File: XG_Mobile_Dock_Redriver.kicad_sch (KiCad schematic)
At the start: 170 parts, among them J1 5-1775443-8, J13 39301240, J14 I2C1, J2 20455-040E-76, J3 20455-040E-76, J4 469911008, J7 10147430-113T0LF, SW1 SW_Push, U1 DS320PR810NJXR, U2 DS320PR810NJXR, U7 TPS7A8400ARGRR, U8 TPS7A8400ARGRR

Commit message: smaller caps
smaller caps
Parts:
- C62, C68, C69, C70: footprint Capacitor_SMD:C_0805_2012Metric -> Capacitor_SMD:C_0402_1005Metric; LCSC C1710 -> C15195; Part_Number CL21B103KBANNNC -> CL05B103KB5NNNC
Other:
- note added: "10nf CL05B103KB5NNNC Mfpart C15195 LCSC 0402 100nF GRM033R61C104KE84D MfPart C76937 LCSC 220nF GRM033R61C224KE14D MfPart C161474 LCSC 1uf CL03A105MO3NRNH MfPart C307385 LCSC 10uF CL10A106KP8NNNC MfPart C19702 LCSC 47uF CL31A476MPHNNNE MfPart C96123 LCSC 1206 1k RC0603JR-071KL MfPart C14676 LCSC L0 8.25k 0603WAF8251T5E MfPart C23113 LCSC L1 24.9k RC0603FR-0724K9L MfPart C137761 LCSC L2 75k 0603WAF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"
- note removed: "10nf CL21B103KBANNNC Mfpart C1710 LCSC 0805 100nF GRM033R61C104KE84D MfPart C76937 LCSC 220nF GRM033R61C224KE14D MfPart C161474 LCSC 1uf CL03A105MO3NRNH MfPart C307385 LCSC 10uF CL10A106KP8NNNC MfPart C19702 LCSC 47uF CL31A476MPHNNNE MfPart C96123 LCSC 1206 1k RC0603JR-071KL MfPart C14676 LCSC L0 8.25k 0603WAF8251T5E MfPart C23113 LCSC L1 24.9k RC0603FR-0724K9L MfPart C137761 LCSC L2 75k 0603WAF7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"
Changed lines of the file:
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@@
 	(generator_version "9.0")
 	(paper "A3")
-	(text "10nf CL21B103KBANNNC Mfpart C1710 LCSC 0805\n100nF GRM033R61C104KE84D MfPart C76937 LCSC\n220nF GRM033R61C224KE14D MfPart C161474 LCSC\n1uf CL03A105MO3NRNH MfPart C307385 LCSC \n10uF CL10A106KP8NNNC MfPart C19702 LCSC\n47uF CL31A476MPHNNNE MfPart C96123 LCSC 1206\n1k RC0603JR-071KL MfPart C14676 LCSC L0\n8.25k 0603WAF8251T5E MfPart C23113 LCSC L1\n24.9k RC0603FR-0724K9L MfPart C137761 LCSC L2\n75k 0603WAF7502T5E MfPart C23242 LCSC L3\n4.7k 0402WGF4701TCE MfPart C25900 LCSC 0402"
+	(text "10nf CL05B103KB5NNNC Mfpart C15195 LCSC 0402\n100nF GRM033R61C104KE84D MfPart C76937 LCSC\n220nF GRM033R61C224KE14D MfPart C161474 LCSC\n1uf CL03A105MO3NRNH MfPart C307385 LCSC \n10uF CL10A106KP8NNNC MfPart C19702 LCSC\n47uF CL31A476MPHNNNE MfPart C96123 LCSC 1206\n1k RC0603JR-071KL MfPart C14676 LCSC L0\n8.25k 0603WAF8251T5E MfPart C23113 LCSC L1\n24.9k RC0603FR-0724K9L MfPart C137761 LCSC L2\n75k 0603WAF7502T5E MfPart C23242 LCSC L3\n4.7k 0402WGF4701TCE MfPart C25900 LCSC 0402"
 		(exclude_from_sim no)
 		(at 377.952 23.368 0)
@@
 			)
 		)
-		(property "Footprint" "Capacitor_SMD:C_0805_2012Metric"
+		(property "Footprint" "Capacitor_SMD:C_0402_1005Metric"
 			(at 456.2348 24.13 0)
 			(effects
@@
 			)
 		)
-		(property "Part_Number" "CL21B103KBANNNC"
+		(property "Part_Number" "CL05B103KB5NNNC"
 			(at 457.2 20.32 0)
 			(effects
@@
 			)
 		)
-		(property "LCSC" "C1710"
+		(property "LCSC" "C15195"
 			(at 457.2 20.32 0)
 			(effects
@@
 			)
 		)
-		(property "Footprint" "Capacitor_SMD:C_0805_2012Metric"
+		(property "Footprint" "Capacitor_SMD:C_0402_1005Metric"
 			(at 449.8848 95.25 0)
 			(effects
@@
 			)
 		)
-		(property "Part_Number" "CL21B103KBANNNC"
+		(property "Part_Number" "CL05B103KB5NNNC"
 			(at 450.85 91.44 0)
 			(effects
@@
 			)
 		)
-		(property "LCSC" "C1710"
+		(property "LCSC" "C15195"
 			(at 450.85 91.44 0)
 			(effects
@@
 			)
 		)
-		(property "Footprint" "Capacitor_SMD:C_0805_2012Metric"
+		(property "Footprint" "Capacitor_SMD:C_0402_1005Metric"
 			(at 504.4948 30.48 0)
 			(effects
@@
 			)
 		)
-		(property "Part_Number" "CL21B103KBANNNC"
+		(property "Part_Number" "CL05B103KB5NNNC"
 			(at 505.46 26.67 0)
 			(effects
@@
 			)
 		)
-		(property "LCSC" "C1710"
+		(property "LCSC" "C15195"
 			(at 505.46 26.67 0)
 			(effects
@@
 			)
 		)
-		(property "Footprint" "Capacitor_SMD:C_0805_2012Metric"
+		(property "Footprint" "Capacitor_SMD:C_0402_1005Metric"
 			(at 498.1448 101.6 0)
 			(effects
@@
 			)
 		)
-		(property "Part_Number" "CL21B103KBANNNC"
+		(property "Part_Number" "CL05B103KB5NNNC"
 			(at 499.11 97.79 0)
 			(effects
@@
 			)
 		)
-		(property "LCSC" "C1710"
+		(property "LCSC" "C15195"
 			(at 499.11 97.79 0)
 			(effects

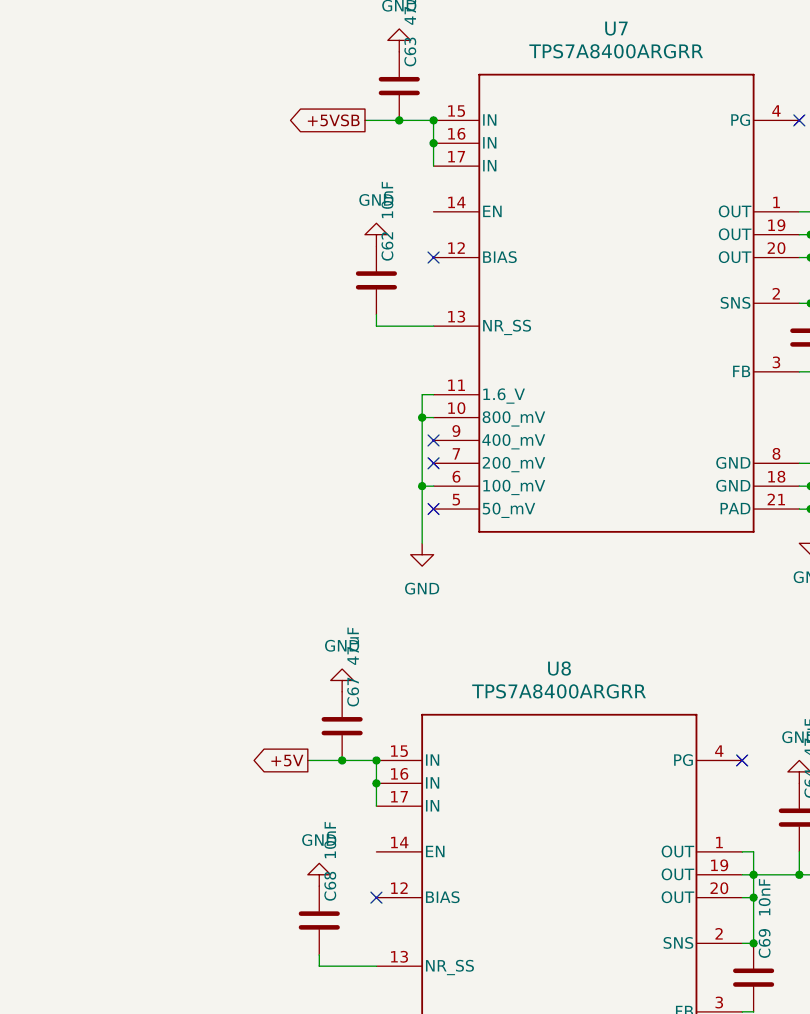
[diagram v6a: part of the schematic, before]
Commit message: enable ldo
enable ldo
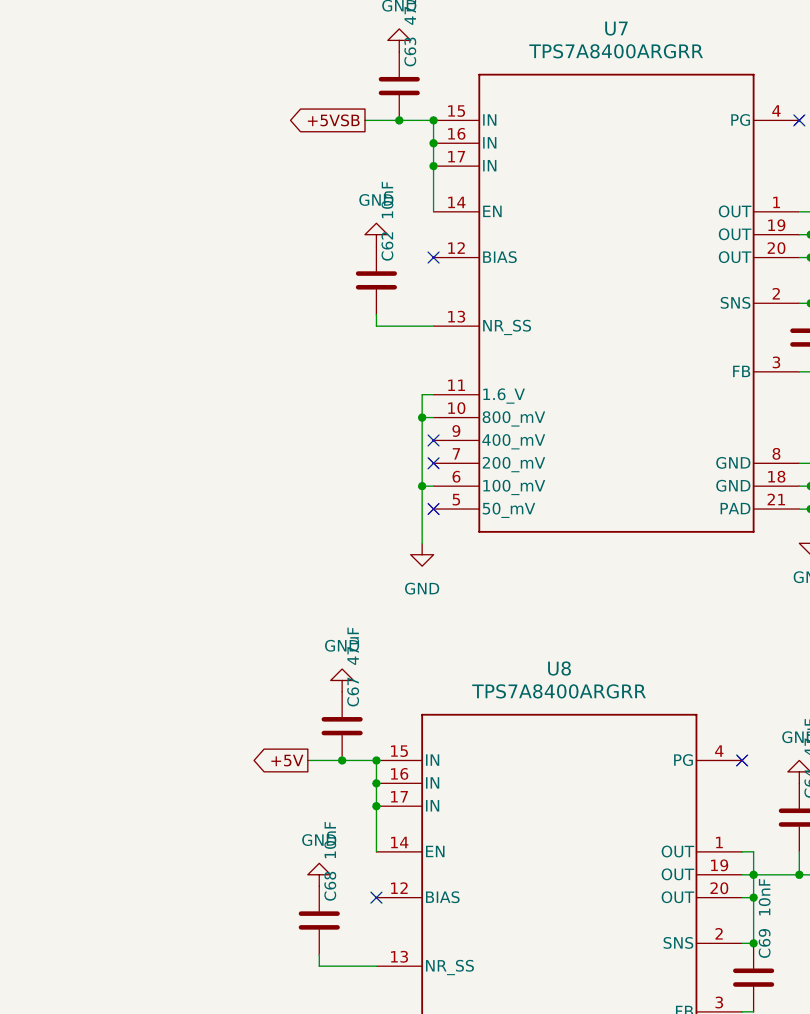
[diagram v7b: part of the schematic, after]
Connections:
- net +5V: now also U8.14 (EN)
- net +5VSB: now also U7.14 (EN)
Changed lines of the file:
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@@
 	)
 	(junction
+		(at 463.55 7.62)
+		(diameter 0)
+		(color 0 0 0 0)
+	)
+	(junction
 		(at 283.21 124.46)
 		(diameter 0)
@@
 	)
 	(junction
+		(at 457.2 78.74)
+		(diameter 0)
+		(color 0 0 0 0)
+	)
+	(junction
 		(at 283.21 91.44)
 		(diameter 0)
@@
 	(wire
 		(pts
+			(xy 463.55 7.62) (xy 463.55 12.7)
+		)
+		(stroke
+			(width 0)
+			(type default)
+		)
+	)
+	(wire
+		(pts
 			(xy 170.18 224.79) (xy 182.88 224.79)
 		)
@@
 		)
 		(stroke
+			(width 0)
+			(type default)
+		)
+	)
+	(wire
+		(pts
+			(xy 457.2 78.74) (xy 457.2 83.82)
+		)
+		(stroke

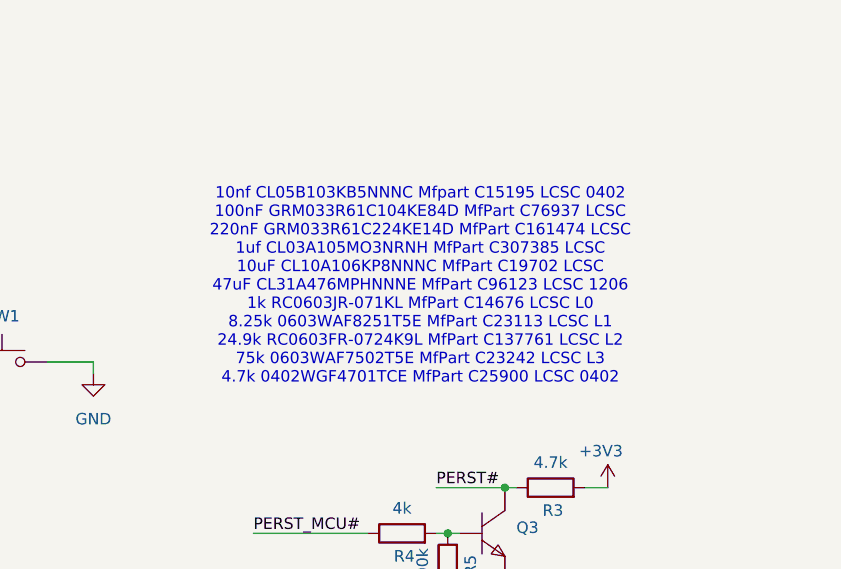
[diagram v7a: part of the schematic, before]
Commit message: added 0805 caps
added 0805 caps
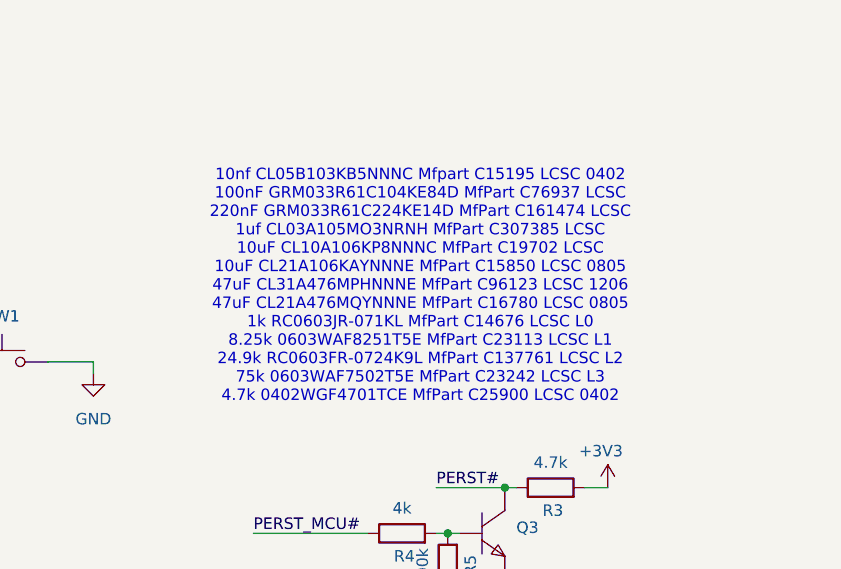
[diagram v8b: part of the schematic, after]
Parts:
- C63, C64, C67, C71: footprint Capacitor_SMD:C_1206_3216Metric -> Capacitor_SMD:C_0805_2012Metric; LCSC C96123 -> C16780; Part_Number CL31A476MPHNNNE -> CL21A476MQYNNNE
- C65, C66, C72, C73: footprint Capacitor_SMD:C_0603_1608Metric -> Capacitor_SMD:C_0805_2012Metric; LCSC C19702 -> C15850; Part_Number CL10A106KP8NNNC -> CL21A106KAYNNNE
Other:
- note added: "10nf CL05B103KB5NNNC Mfpart C15195 LCSC 0402 100nF GRM033R61C104KE84D MfPart C76937 LCSC 220nF GRM033R61C224KE14D MfPart C161474 LCSC 1uf CL03A105MO3NRNH MfPart C307385 LCSC 10uF CL10A106KP8NNNC MfPart C19702 LCSC 10uF CL21A106KAYNNNE MfPart C15850 LCSC 0805 47uF CL31A476MPHNNNE MfPart C96123 LCSC 1206 47uF CL21A476MQYNNNE MfPart C16780 LCSC 0805 1k RC0603JR-071KL MfPart C14676 LCSC L0 8.25k 0603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"
- note removed: "10nf CL05B103KB5NNNC Mfpart C15195 LCSC 0402 100nF GRM033R61C104KE84D MfPart C76937 LCSC 220nF GRM033R61C224KE14D MfPart C161474 LCSC 1uf CL03A105MO3NRNH MfPart C307385 LCSC 10uF CL10A106KP8NNNC MfPart C19702 LCSC 47uF CL31A476MPHNNNE MfPart C96123 LCSC 1206 1k RC0603JR-071KL MfPart C14676 LCSC L0 8.25k 0603WAF8251T5E MfPart C23113 LCSC L1 24.9k RC0603FR-0724K9L MfPart C137761 LCSC L2 75k 0603WAF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"
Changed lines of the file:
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@@
 	(generator_version "9.0")
 	(paper "A3")
-	(text "10nf CL05B103KB5NNNC Mfpart C15195 LCSC 0402\n100nF GRM033R61C104KE84D MfPart C76937 LCSC\n220nF GRM033R61C224KE14D MfPart C161474 LCSC\n1uf CL03A105MO3NRNH MfPart C307385 LCSC \n10uF CL10A106KP8NNNC MfPart C19702 LCSC\n47uF CL31A476MPHNNNE MfPart C96123 LCSC 1206\n1k RC0603JR-071KL MfPart C14676 LCSC L0\n8.25k 0603WAF8251T5E MfPart C23113 LCSC L1\n24.9k RC0603FR-0724K9L MfPart C137761 LCSC L2\n75k 0603WAF7502T5E MfPart C23242 LCSC L3\n4.7k 0402WGF4701TCE MfPart C25900 LCSC 0402"
+	(text "10nf CL05B103KB5NNNC Mfpart C15195 LCSC 0402\n100nF GRM033R61C104KE84D MfPart C76937 LCSC\n220nF GRM033R61C224KE14D MfPart C161474 LCSC\n1uf CL03A105MO3NRNH MfPart C307385 LCSC \n10uF CL10A106KP8NNNC MfPart C19702 LCSC\n10uF CL21A106KAYNNNE MfPart C15850 LCSC 0805\n47uF CL31A476MPHNNNE MfPart C96123 LCSC 1206\n47uF CL21A476MQYNNNE MfPart C16780 LCSC 0805\n1k RC0603JR-071KL MfPart C14676 LCSC L0\n8.25k 0603WAF8251T5E MfPart C23113 LCSC L1\n24.9k RC0603FR-0724K9L MfPart C137761 LCSC L2\n75k 0603WAF7502T5E MfPart C23242 LCSC L3\n4.7k 0402WGF4701TCE MfPart C25900 LCSC 0402"
 		(exclude_from_sim no)
 		(at 377.952 23.368 0)
@@
 			)
 		)
-		(property "Footprint" "Capacitor_SMD:C_1206_3216Metric"
+		(property "Footprint" "Capacitor_SMD:C_0805_2012Metric"
 			(at 458.7748 2.54 0)
 			(effects
@@
 			)
 		)
-		(property "Part_Number" "CL31A476MPHNNNE"
+		(property "Part_Number" "CL21A476MQYNNNE"
 			(at 459.74 -1.27 0)
 			(effects
@@
 			)
 		)
-		(property "LCSC" "C96123"
+		(property "LCSC" "C16780"
 			(at 459.74 -1.27 0)
 			(effects
@@
 			)
 		)
-		(property "Footprint" "Capacitor_SMD:C_1206_3216Metric"
+		(property "Footprint" "Capacitor_SMD:C_0805_2012Metric"
 			(at 452.4248 73.66 0)
 			(effects
@@
 			)
 		)
-		(property "Part_Number" "CL31A476MPHNNNE"
+		(property "Part_Number" "CL21A476MQYNNNE"
 			(at 453.39 69.85 0)
 			(effects
@@
 			)
 		)
-		(property "LCSC" "C96123"
+		(property "LCSC" "C16780"
 			(at 453.39 69.85 0)
 			(effects
@@
 			)
 		)
-		(property "Footprint" "Capacitor_SMD:C_0603_1608Metric"
+		(property "Footprint" "Capacitor_SMD:C_0805_2012Metric"
 			(at 513.3848 83.82 0)
 			(effects
@@
 			)
 		)
-		(property "Part_Number" "CL10A106KP8NNNC"
+		(property "Part_Number" "CL21A106KAYNNNE"
 			(at 514.35 80.01 0)
 			(effects
@@
 			)
 		)
-		(property "LCSC" "C19702"
+		(property "LCSC" "C15850"
 			(at 514.35 80.01 0)
 			(effects
@@
 			)
 		)
-		(property "Footprint" "Capacitor_SMD:C_0603_1608Metric"
+		(property "Footprint" "Capacitor_SMD:C_0805_2012Metric"
 			(at 514.6548 12.7 0)
 			(effects
@@
 			)
 		)
-		(property "Part_Number" "CL10A106KP8NNNC"
+		(property "Part_Number" "CL21A106KAYNNNE"
 			(at 515.62 8.89 0)
 			(effects
@@
 			)
 		)
-		(property "LCSC" "C19702"
+		(property "LCSC" "C15850"
 			(at 515.62 8.89 0)
 			(effects
@@
 			)
 		)
-		(property "Footprint" "Capacitor_SMD:C_0603_1608Metric"
+		(property "Footprint" "Capacitor_SMD:C_0805_2012Metric"
 			(at 508.3048 83.82 0)
 			(effects
@@
 			)
 		)
-		(property "Part_Number" "CL10A106KP8NNNC"
+		(property "Part_Number" "CL21A106KAYNNNE"
 			(at 509.27 80.01 0)
 			(effects
@@
 			)
 		)
-		(property "LCSC" "C19702"
+		(property "LCSC" "C15850"
 			(at 509.27 80.01 0)
 			(effects
@@
 			)
 		)
-		(property "Footprint" "Capacitor_SMD:C_1206_3216Metric"
+		(property "Footprint" "Capacitor_SMD:C_0805_2012Metric"
 			(at 503.2248 83.82 0)
 			(effects
@@
 			)
 		)
-		(property "Part_Number" "CL31A476MPHNNNE"
+		(property "Part_Number" "CL21A476MQYNNNE"
 			(at 504.19 80.01 0)
 			(effects
@@
 			)
 		)
-		(property "LCSC" "C96123"
+		(property "LCSC" "C16780"
 			(at 504.19 80.01 0)
 			(effects
@@
 			)
 		)
-		(property "Footprint" "Capacitor_SMD:C_1206_3216Metric"
+		(property "Footprint" "Capacitor_SMD:C_0805_2012Metric"
 			(at 509.5748 12.7 0)
 			(effects
@@
 			)
 		)
-		(property "Part_Number" "CL31A476MPHNNNE"
+		(property "Part_Number" "CL21A476MQYNNNE"
 			(at 510.54 8.89 0)
 			(effects
@@
 			)
 		)
-		(property "LCSC" "C96123"
+		(property "LCSC" "C16780"
 			(at 510.54 8.89 0)
 			(effects
@@
 			)
 		)
-		(property "Footprint" "Capacitor_SMD:C_0603_1608Metric"
+		(property "Footprint" "Capacitor_SMD:C_0805_2012Metric"
 			(at 519.7348 12.7 0)
 			(effects
@@
 			)
 		)
-		(property "Part_Number" "CL10A106KP8NNNC"
+		(property "Part_Number" "CL21A106KAYNNNE"
 			(at 520.7 8.89 0)
 			(effects
@@
 			)
 		)
-		(property "LCSC" "C19702"
+		(property "LCSC" "C15850"
 			(at 520.7 8.89 0)
 			(effects
